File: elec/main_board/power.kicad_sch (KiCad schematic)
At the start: 43 parts, among them J10 Conn_01x02, J11 B2B-XH-A(LF)(SN), J12 B2B-XH-A(LF)(SN), J16 B4B-ZR(LF)(SN), J9 MJ-179PH, Q5 DMT6008LFG, Q6 DMT6008LFG, Q7 DTC114E, Q8 DTC114E, SW1 SS-22SBH2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

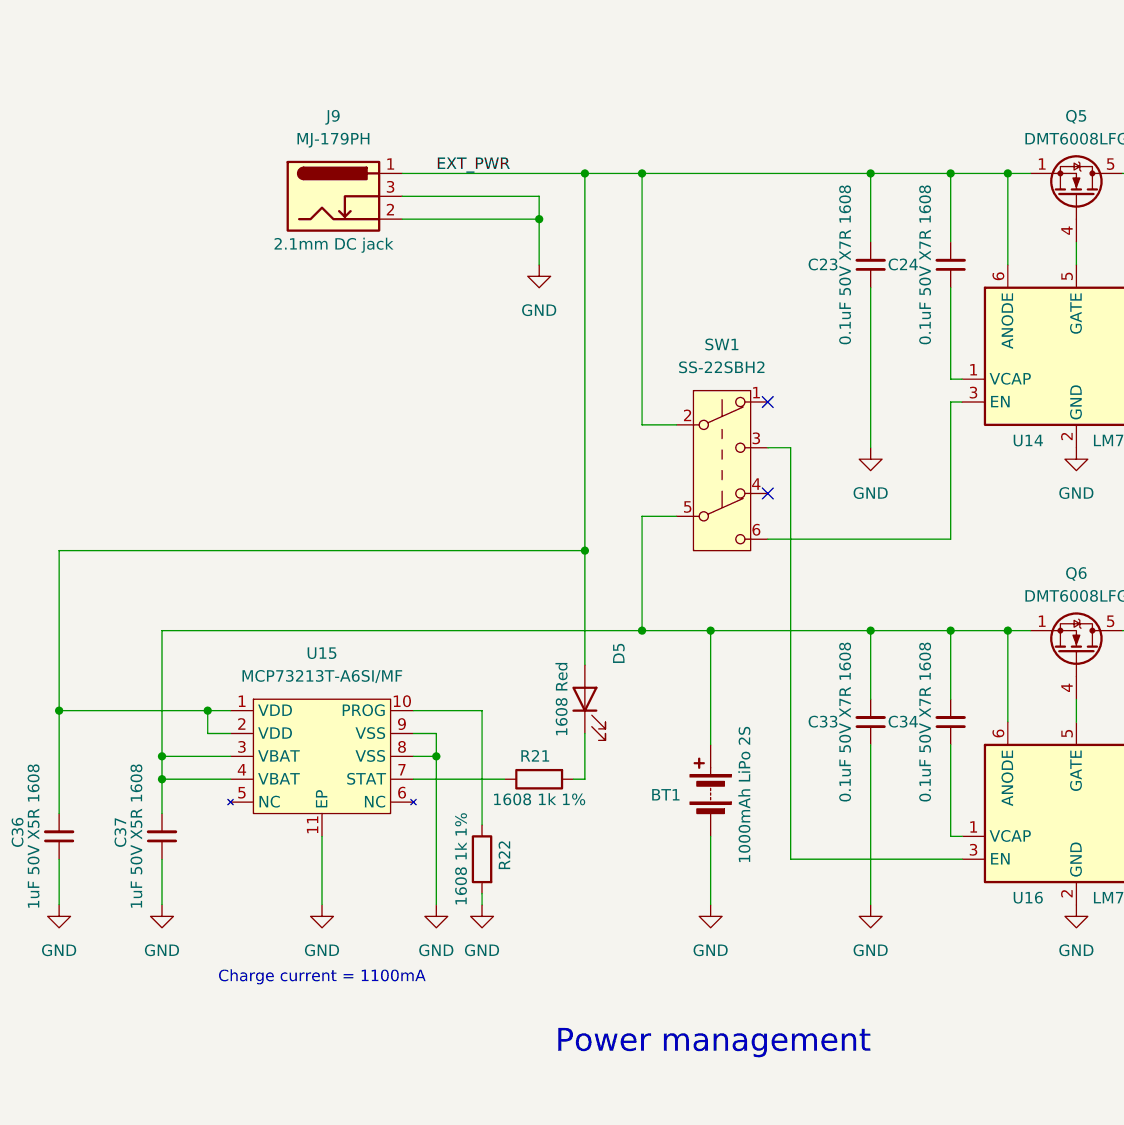
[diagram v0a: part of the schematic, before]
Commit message: 回路図更新
・壁センサLEDの抵抗値を100Ωに変更
・電源スイッチを削除
・ESP32のENにプルアップ追加

Signed-off-by: Kazuki Iida <elkel53930@gmail.com>
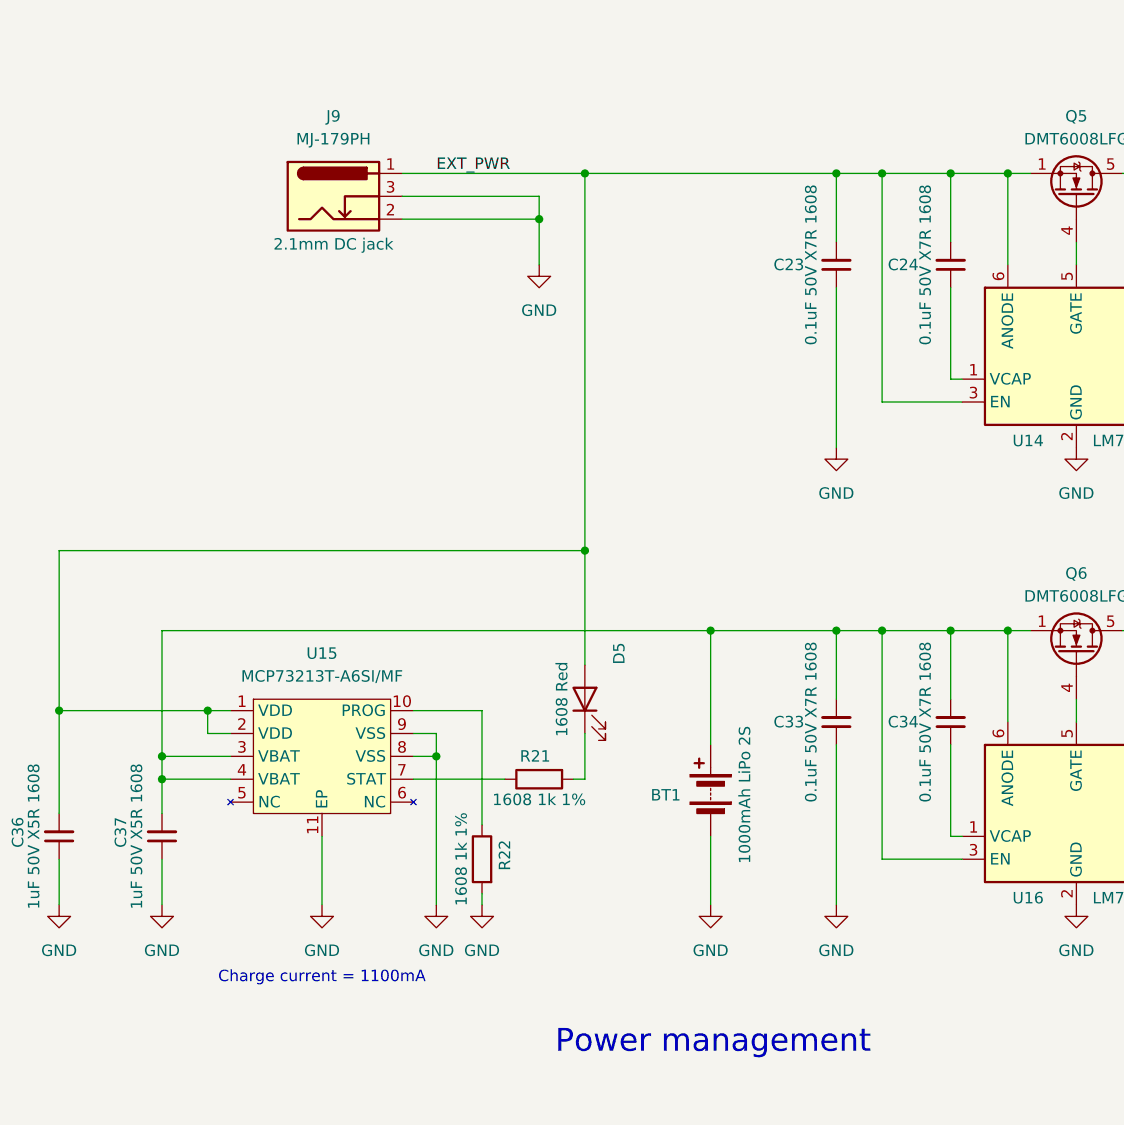
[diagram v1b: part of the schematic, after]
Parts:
- removed SW1: SS-22SBH2, Library:SS-22SBH2, symbol Switch:SW_Push_DPDT
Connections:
- net EXT_PWR: now also U14.3 (EN)
- net at BT1.1 (+), C33.2, C34.2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: now also U16.3 (EN)
- no-connect marks 12 -> 10
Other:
- moved on the sheet: C23, C33
